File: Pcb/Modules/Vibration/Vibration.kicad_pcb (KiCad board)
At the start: 2 copper layers, 49.5 x 21.6 mm, 10 parts, among them J1 JACK_RJ45, P1 C+, P2 C-

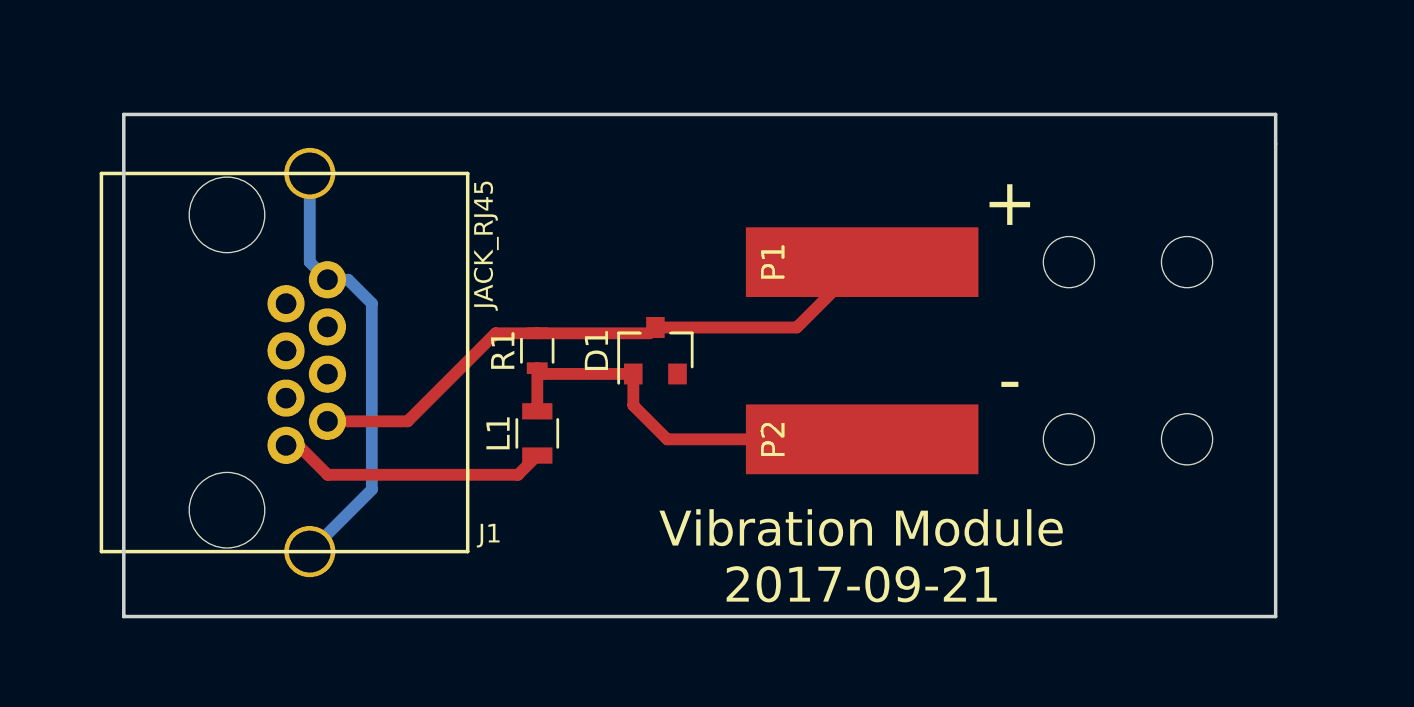
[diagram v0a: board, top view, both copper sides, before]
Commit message: Update vibration module pcb
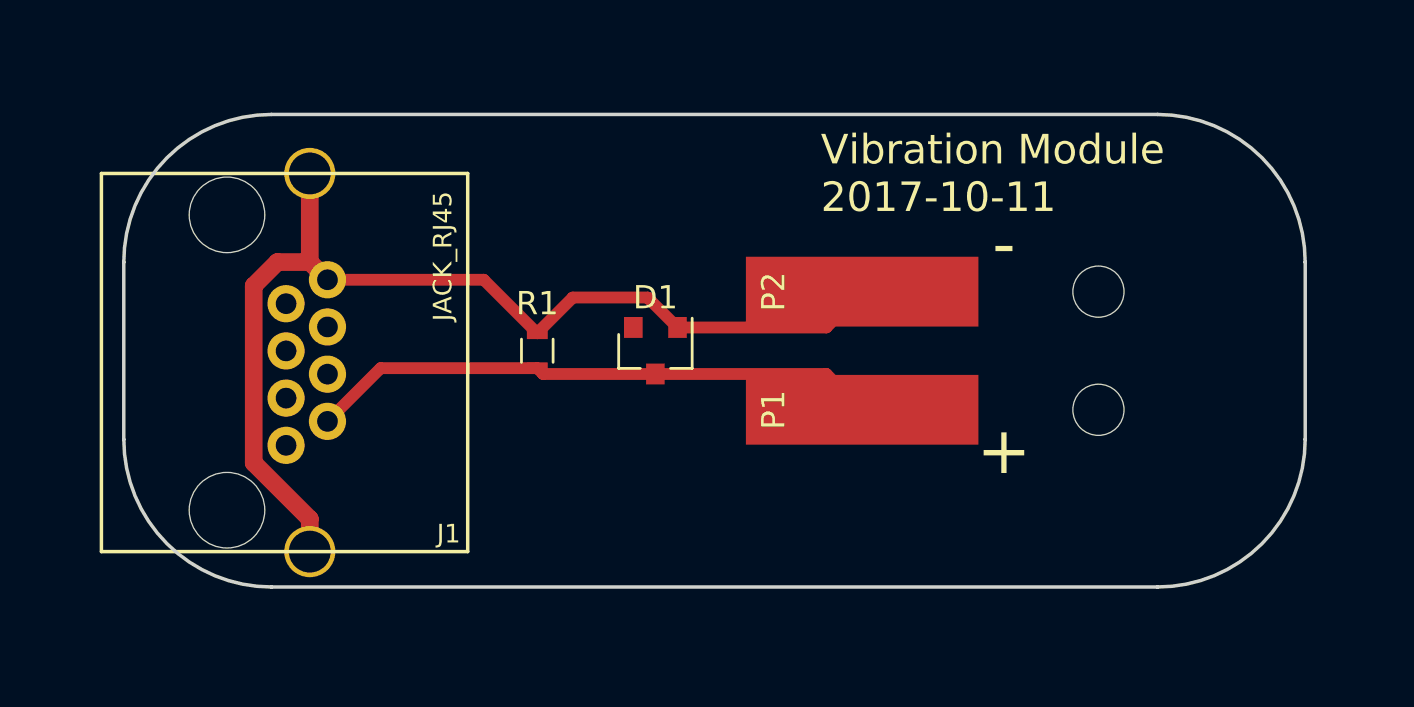
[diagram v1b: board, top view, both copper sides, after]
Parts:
- removed L1: Ferrite_Bead, Resistors_SMD:R_0805
- removed ref123 (x4): MountingHole_2.2mm_M2, Mounting_Holes:MountingHole_2.2mm_M2
- added REF**: MountingHole_2.2mm_M2, Mounting_Holes:MountingHole_2.2mm_M2, F.Cu at (67.3, 33.0)
- added REF**: MountingHole_2.2mm_M2, Mounting_Holes:MountingHole_2.2mm_M2, F.Cu at (67.3, 38.1)
- moved P1 6.35 mm to (57.1, 38.1)
- moved P2 6.35 mm to (57.1, 33.0)
- turned D1 to 270 degrees
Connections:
- J1 pad 1: Net-(J1-Pad1) -> (no net)
- J1 pad 8: Net-(J1-Pad8) -> GND
- R1 pad 1: GND -> Net-(D1-Pad1)
- R1 pad 2: Net-(D1-Pad1) -> GND
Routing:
- net GND: track 17.9 -> 46.1 mm
- net Net-(J1-Pad8): track 19.0 -> 0.00 mm
- net Net-(J1-Pad1): track 11.7 -> 0.00 mm
- net Net-(D1-Pad1): track 25.8 -> 25.0 mm
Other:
- board size 49.5 x 21.6 mm -> 50.8 x 20.3 mm
- net class Default: clearance 0.254 -> 0.2032; trace_width 0.508 -> 0.254; via_dia 0.6 -> 0.6604; via_drill 0.4 -> 0.3556
- rule trace_clearance: 0.254 -> 0.2032
- board text added: "Vibration Module 2017-10-11"
- board text removed: "Vibration Module 2017-09-21"

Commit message: Fix up PCB traces
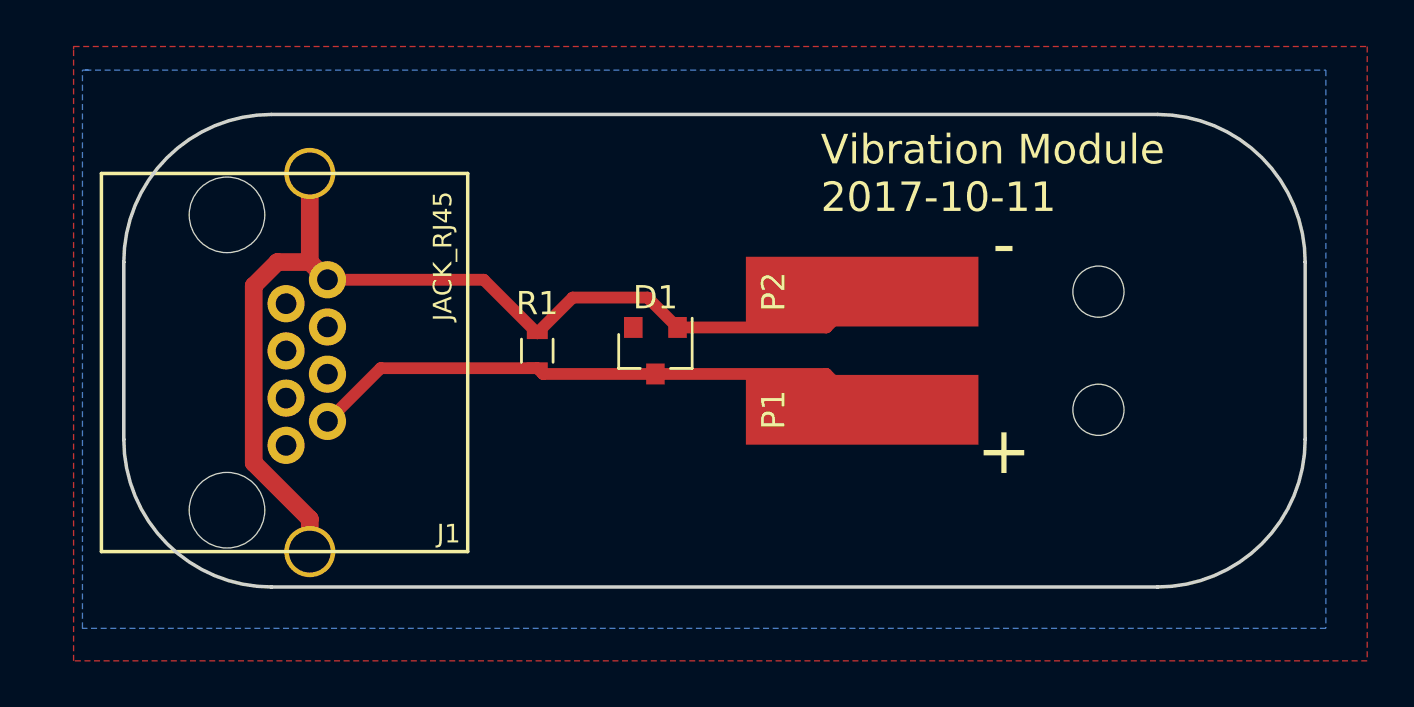
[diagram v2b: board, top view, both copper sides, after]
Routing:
- added copper zone on B.Cu, net GND
- added copper zone on F.Cu, net GND
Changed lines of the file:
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@@
     (links 8)
     (no_connects 0)
-    (area 25.324999 25.324999 164.921001 48.843001)
+    (area 25.324999 25.324999 76.275001 45.795001)
     (thickness 1.6)
     (drawings 11)
@@
   )
   (setup
-    (last_trace_width 0.508)
+    (last_trace_width 0.254)
     (user_trace_width 0.508)
     (user_trace_width 0.762)
     (trace_clearance 0.2032)
-    (zone_clearance 0.254)
+    (zone_clearance 0.508)
     (zone_45_only yes)
     (trace_min 0.2)
@@
   (segment (start 55.61 36.56) (end 57.15 38.1) (width 0.508) (layer F.Cu) (net 2) (status 20))
   (segment (start 48.01 36.31) (end 48.26 36.56) (width 0.254) (layer F.Cu) (net 2) (status 30))
+  (zone (net 1) (net_name GND) (layer F.Cu) (hatch edge 0.508)
+    (connect_pads (clearance 0.508))
+    (min_thickness 0.254)
+    (fill yes (arc_segments 16) (thermal_gap 0.508) (thermal_bridge_width 0.508))
+    (polygon
+      (pts
+        (xy 23.241 22.479) (xy 78.867 22.479) (xy 78.867 48.895) (xy 23.241 48.895) (xy 23.241 22.606)
+      )
+    )
+  )
+  (zone (net 1) (net_name GND) (layer B.Cu) (hatch edge 0.508)
+    (connect_pads (clearance 0.508))
+    (min_thickness 0.254)
+    (fill yes (arc_segments 16) (thermal_gap 0.508) (thermal_bridge_width 0.508))
+    (polygon
+      (pts
+        (xy 23.749 23.495) (xy 77.089 23.495) (xy 77.089 47.498) (xy 23.622 47.498) (xy 23.622 23.495)
+        (xy 23.876 23.495)
+      )
+    )
+  )
 )

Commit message: Update pcb layout for modules
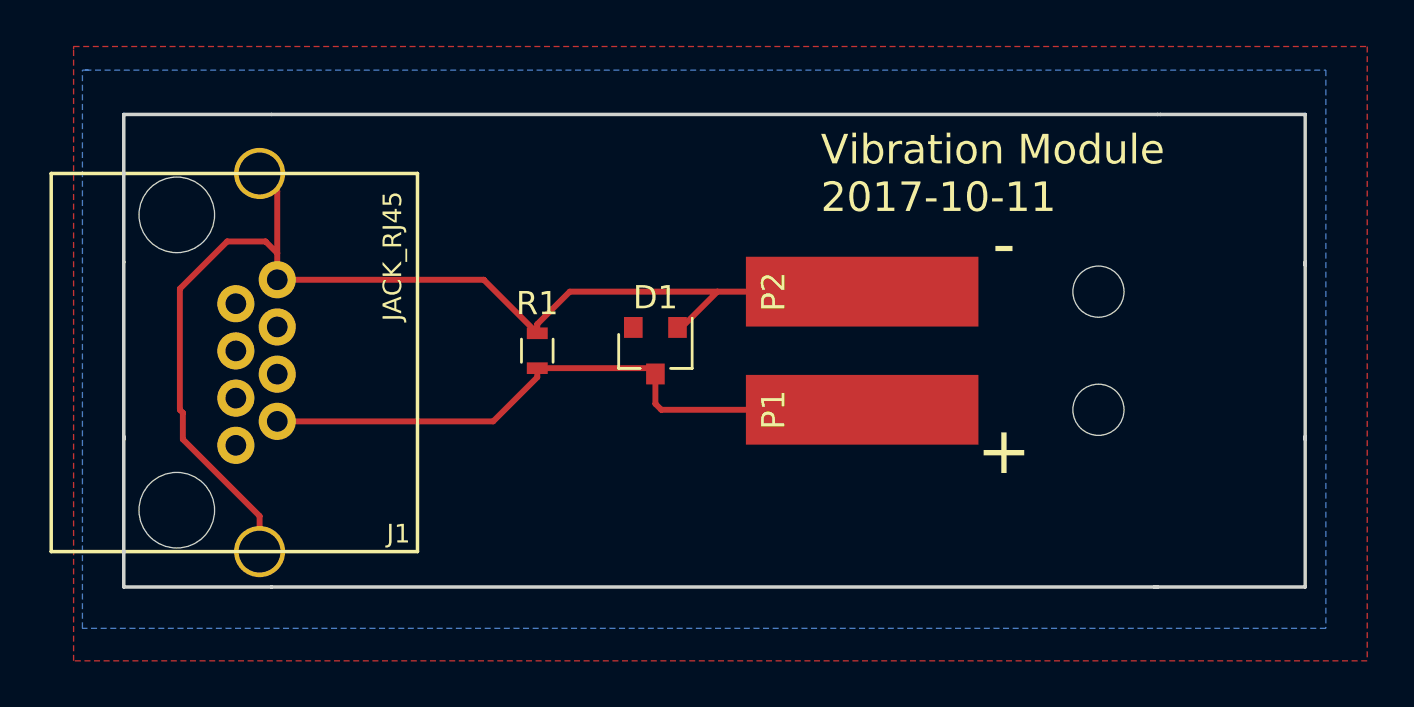
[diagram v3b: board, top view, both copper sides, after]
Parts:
- moved J1 2.16 mm to (30.1, 36.1)
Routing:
- net GND: track 46.1 -> 52.3 mm
- net Net-(D1-Pad1): track 25.0 -> 27.8 mm
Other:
- outline, holes or cut-outs redrawn
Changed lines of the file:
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@@
-(kicad_pcb (version 4) (host pcbnew 4.0.5)
+(kicad_pcb (version 4) (host pcbnew 4.0.7)
   (general
     (links 8)
     (no_connects 0)
-    (area 25.324999 25.324999 76.275001 45.795001)
+    (area 23.241 22.479 78.867001 48.895001)
     (thickness 1.6)
-    (drawings 11)
-    (tracks 23)
+    (drawings 16)
+    (tracks 27)
     (zones 0)
     (modules 7)
@@
   )
   (module CA6:RJ45_pcbwing (layer F.Cu)
-    (at 32.258 36.068 270)
+    (at 30.099 36.068 270)
     (fp_text reference J1 (at 7.366 -7.112 360) (layer F.SilkS)
       (effects (font (size 0.8 0.8) (thickness 0.15)))
@@
     (pad 1 np_thru_hole circle (at 0 0) (size 2.2 2.2) (drill 2.2) (layers *.Cu *.Mask))
   )
+  (gr_line (start 25.4 25.4) (end 31.75 25.4) (angle 90) (layer Edge.Cuts) (width 0.15))
+  (gr_line (start 25.4 31.75) (end 25.4 25.4) (angle 90) (layer Edge.Cuts) (width 0.15))
+  (gr_line (start 25.4 45.72) (end 25.4 39.243) (angle 90) (layer Edge.Cuts) (width 0.15))
+  (gr_line (start 31.75 45.72) (end 25.4 45.72) (angle 90) (layer Edge.Cuts) (width 0.15))
+  (gr_line (start 69.977 25.4) (end 69.85 25.4) (angle 90) (layer Edge.Cuts) (width 0.15))
+  (gr_line (start 76.2 25.4) (end 76.2 31.877) (angle 90) (layer Edge.Cuts) (width 0.15))
+  (gr_line (start 69.977 25.4) (end 76.2 25.4) (angle 90) (layer Edge.Cuts) (width 0.15))
+  (gr_line (start 76.2 45.72) (end 76.2 39.243) (angle 90) (layer Edge.Cuts) (width 0.15))
+  (gr_line (start 69.723 45.72) (end 76.2 45.72) (angle 90) (layer Edge.Cuts) (width 0.15))
   (gr_text + (at 63.246 39.878) (layer F.SilkS)
     (effects (font (size 2.032 2.032) (thickness 0.3)))
@@
     (effects (font (size 1.27 1.27) (thickness 0.254)) (justify left))
   )
-  (gr_arc (start 31.75 39.37) (end 31.75 45.72) (angle 90) (layer Edge.Cuts) (width 0.15))
-  (gr_arc (start 69.85 39.37) (end 76.2 39.37) (angle 90) (layer Edge.Cuts) (width 0.15))
-  (gr_arc (start 69.85 31.75) (end 69.85 25.4) (angle 90) (layer Edge.Cuts) (width 0.15))
-  (gr_arc (start 31.75 31.75) (end 25.4 31.75) (angle 90) (layer Edge.Cuts) (width 0.15))
   (gr_line (start 69.85 45.72) (end 31.75 45.72) (angle 90) (layer Edge.Cuts) (width 0.15))
   (gr_line (start 31.75 25.4) (end 69.85 25.4) (angle 90) (layer Edge.Cuts) (width 0.15))
-  (segment (start 49.21 34.56) (end 55.61 34.56) (width 0.508) (layer F.Cu) (net 1) (status 10))
-  (segment (start 55.61 34.56) (end 57.15 33.02) (width 0.508) (layer F.Cu) (net 1) (status 20))
-  (segment (start 43.18 34.81) (end 43.18 34.798) (width 0.508) (layer F.Cu) (net 1) (status 30))
-  (segment (start 43.18 34.798) (end 44.704 33.274) (width 0.508) (layer F.Cu) (net 1) (status 10))
-  (segment (start 47.924 33.274) (end 49.21 34.56) (width 0.508) (layer F.Cu) (net 1) (status 20))
-  (segment (start 44.704 33.274) (end 47.924 33.274) (width 0.508) (layer F.Cu) (net 1))
-  (segment (start 34.158 32.508) (end 40.878 32.508) (width 0.508) (layer F.Cu) (net 1) (status 10))
-  (segment (start 40.878 32.508) (end 43.18 34.81) (width 0.508) (layer F.Cu) (net 1) (status 20))
-  (segment (start 33.398 44.198) (end 33.398 42.796) (width 0.762) (layer F.Cu) (net 1) (status 10))
-  (segment (start 32.006 31.748) (end 33.398 31.748) (width 0.762) (layer F.Cu) (net 1))
-  (segment (start 30.988 32.766) (end 32.006 31.748) (width 0.762) (layer F.Cu) (net 1))
-  (segment (start 30.988 40.386) (end 30.988 32.766) (width 0.762) (layer F.Cu) (net 1))
-  (segment (start 33.398 42.796) (end 30.988 40.386) (width 0.762) (layer F.Cu) (net 1))
-  (segment (start 33.398 27.938) (end 33.398 31.748) (width 0.762) (layer F.Cu) (net 1) (status 10))
-  (segment (start 33.398 31.748) (end 34.158 32.508) (width 0.762) (layer F.Cu) (net 1) (status 20))
-  (segment (start 43.18 34.81) (end 42.938 34.81) (width 0.254) (layer F.Cu) (net 1) (status 30))
-  (segment (start 43.18 36.31) (end 36.446 36.31) (width 0.508) (layer F.Cu) (net 2) (status 10))
-  (segment (start 36.446 36.31) (end 34.158 38.598) (width 0.508) (layer F.Cu) (net 2) (status 20))
-  (segment (start 48.26 36.56) (end 43.43 36.56) (width 0.508) (layer F.Cu) (net 2) (status 30))
-  (segment (start 43.43 36.56) (end 43.18 36.31) (width 0.508) (layer F.Cu) (net 2) (status 30))
-  (segment (start 48.26 36.56) (end 55.61 36.56) (width 0.508) (layer F.Cu) (net 2) (status 10))
-  (segment (start 55.61 36.56) (end 57.15 38.1) (width 0.508) (layer F.Cu) (net 2) (status 20))
-  (segment (start 48.01 36.31) (end 48.26 36.56) (width 0.254) (layer F.Cu) (net 2) (status 30))
+  (segment (start 31.239 44.198) (end 31.239 42.669) (width 0.254) (layer F.Cu) (net 1))
+  (segment (start 31.496 30.861) (end 31.999 31.364) (width 0.254) (layer F.Cu) (net 1))
+  (segment (start 29.845 30.861) (end 31.496 30.861) (width 0.254) (layer F.Cu) (net 1))
+  (segment (start 27.813 32.893) (end 29.845 30.861) (width 0.254) (layer F.Cu) (net 1))
+  (segment (start 27.813 38.1) (end 27.813 32.893) (width 0.254) (layer F.Cu) (net 1))
+  (segment (start 27.94 38.227) (end 27.813 38.1) (width 0.254) (layer F.Cu) (net 1))
+  (segment (start 27.94 39.37) (end 27.94 38.227) (width 0.254) (layer F.Cu) (net 1))
+  (segment (start 31.239 42.669) (end 27.94 39.37) (width 0.254) (layer F.Cu) (net 1))
+  (segment (start 31.999 32.508) (end 40.878 32.508) (width 0.254) (layer F.Cu) (net 1))
+  (segment (start 40.878 32.508) (end 43.18 34.81) (width 0.254) (layer F.Cu) (net 1))
+  (segment (start 31.999 32.508) (end 31.999 31.364) (width 0.254) (layer F.Cu) (net 1))
+  (segment (start 31.999 31.364) (end 31.999 28.698) (width 0.254) (layer F.Cu) (net 1))
+  (segment (start 31.999 28.698) (end 31.239 27.938) (width 0.254) (layer F.Cu) (net 1))
+  (segment (start 43.18 34.81) (end 43.18 34.417) (width 0.254) (layer F.Cu) (net 1))
+  (segment (start 43.18 34.417) (end 44.577 33.02) (width 0.254) (layer F.Cu) (net 1))
+  (segment (start 44.577 33.02) (end 50.927 33.02) (width 0.254) (layer F.Cu) (net 1))
+  (segment (start 49.21 34.56) (end 49.387 34.56) (width 0.254) (layer F.Cu) (net 1))
+  (segment (start 49.387 34.56) (end 50.927 33.02) (width 0.254) (layer F.Cu) (net 1))
+  (segment (start 50.927 33.02) (end 57.15 33.02) (width 0.254) (layer F.Cu) (net 1))
+  (segment (start 31.999 38.598) (end 41.285 38.598) (width 0.254) (layer F.Cu) (net 2))
+  (segment (start 43.18 36.703) (end 43.18 36.31) (width 0.254) (layer F.Cu) (net 2))
+  (segment (start 41.285 38.598) (end 43.18 36.703) (width 0.254) (layer F.Cu) (net 2))
+  (segment (start 43.18 36.31) (end 48.01 36.31) (width 0.254) (layer F.Cu) (net 2))
+  (segment (start 48.01 36.31) (end 48.26 36.56) (width 0.254) (layer F.Cu) (net 2))
+  (segment (start 48.26 36.56) (end 48.26 37.846) (width 0.254) (layer F.Cu) (net 2))
+  (segment (start 48.514 38.1) (end 57.15 38.1) (width 0.254) (layer F.Cu) (net 2))
+  (segment (start 48.26 37.846) (end 48.514 38.1) (width 0.254) (layer F.Cu) (net 2))
   (zone (net 1) (net_name GND) (layer F.Cu) (hatch edge 0.508)
     (connect_pads (clearance 0.508))

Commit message: Update module pcbs
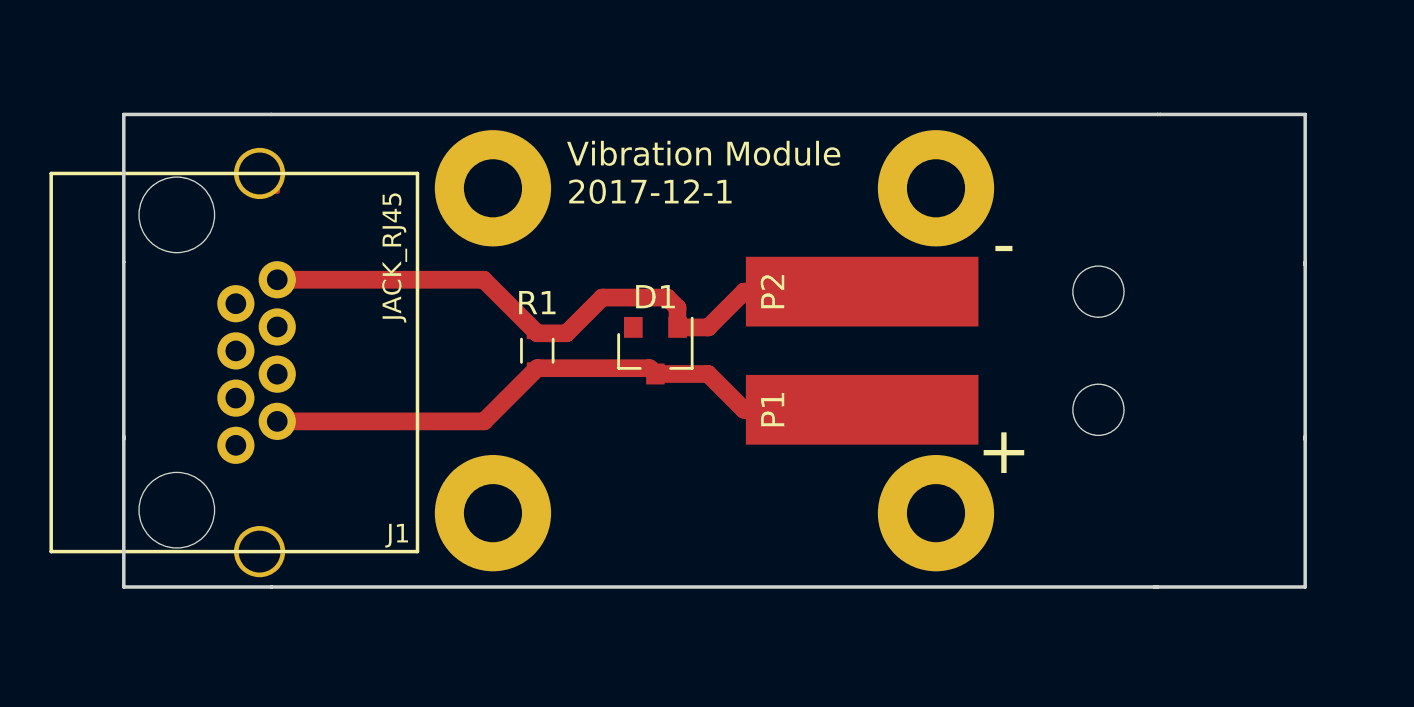
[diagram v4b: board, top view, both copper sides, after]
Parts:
- removed REF** (x2): MountingHole_2.2mm_M2, Mounting_Holes:MountingHole_2.2mm_M2
- added X1: HOLE, Mounting_Holes:MountingHole_2.5mm_Pad, F.Cu at (60.3, 42.5)
- added X2: HOLE, Mounting_Holes:MountingHole_2.5mm_Pad, F.Cu at (41.3, 28.6)
- added X3: HOLE, Mounting_Holes:MountingHole_2.2mm_M2, F.Cu at (67.3, 38.1)
- added X4: HOLE, Mounting_Holes:MountingHole_2.2mm_M2, F.Cu at (67.3, 33.0)
- added X5: HOLE, Mounting_Holes:MountingHole_2.5mm_Pad, F.Cu at (60.3, 28.6)
- added X6: HOLE, Mounting_Holes:MountingHole_2.5mm_Pad, F.Cu at (41.3, 42.5)
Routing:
- net GND: track 52.3 -> 29.7 mm
- net Net-(D1-Pad1): track 27.8 -> 27.2 mm
- removed copper zone on F.Cu, net GND
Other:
- board text added: "Vibration Module 2017-12-1"
- board text removed: "Vibration Module 2017-10-11"
